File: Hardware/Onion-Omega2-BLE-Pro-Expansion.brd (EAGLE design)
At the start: 60 x 50 mm, 37 parts, among them J1 USB-MICROB, J2 USB-A-H, U2 ONION-OMEGA2

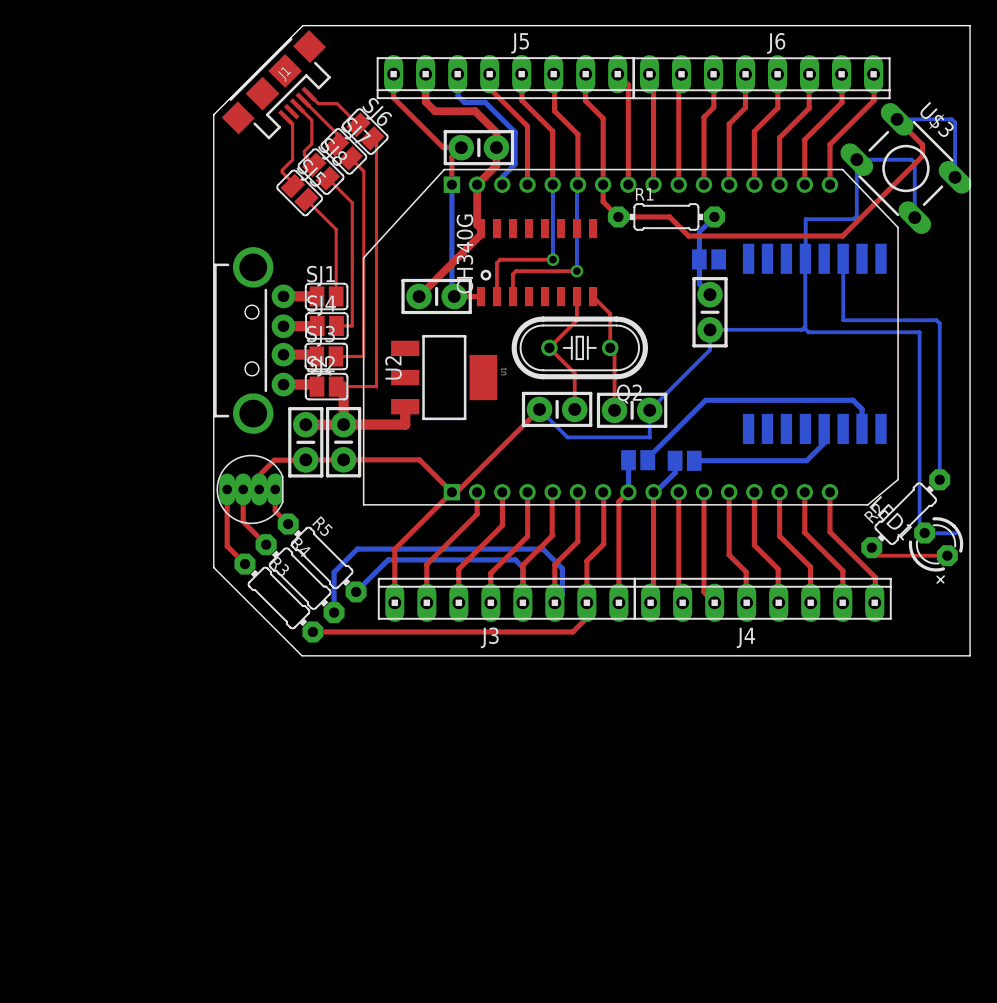
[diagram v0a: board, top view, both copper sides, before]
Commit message: Board Size reduced. Replaced almost all PTH with SMD. CH340G breakout. Minor improvements. Halfway manual routing. Lots of DRC errors
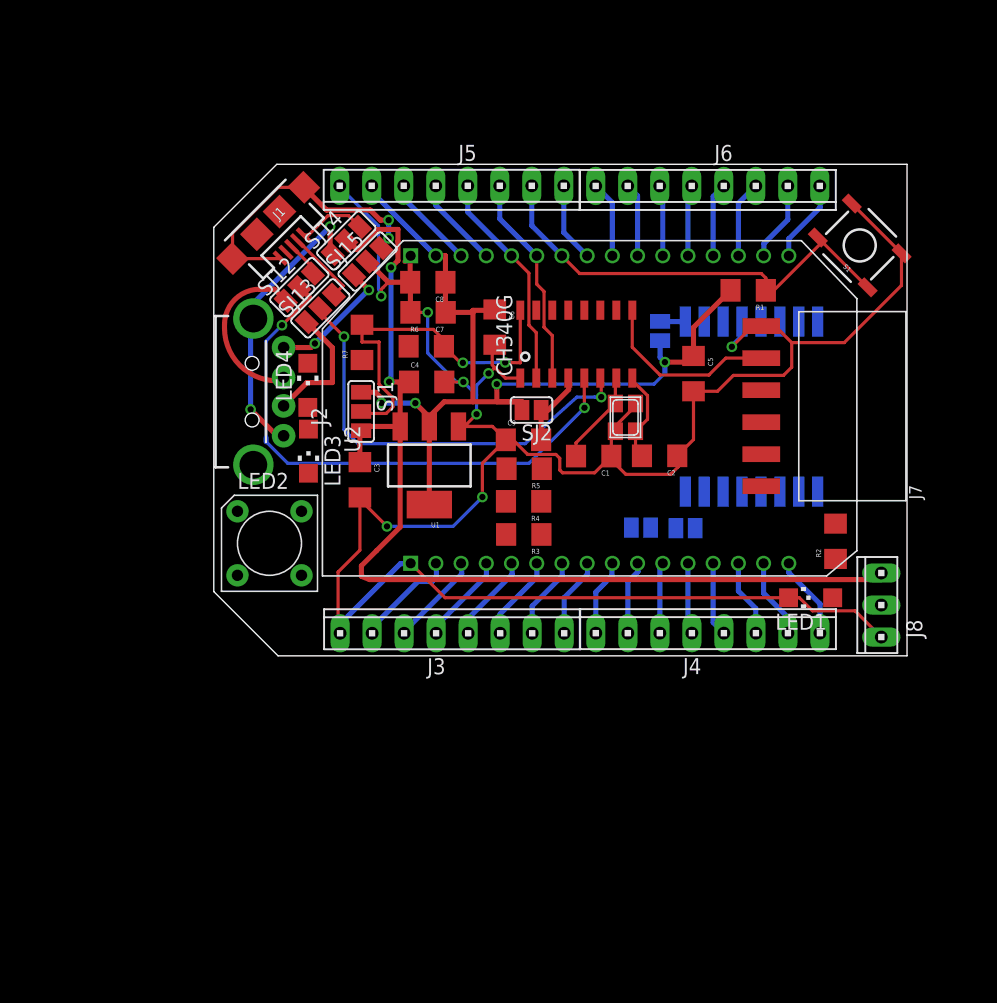
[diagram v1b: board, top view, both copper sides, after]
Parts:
- removed D1: LED-RGB-CC-THRUCLEAR, SparkFun-LED:LED-RGB-THRU
- removed Q2: (no value), adafruit:HC49U-V
- removed SJ3, SJ4, SJ5, SJ6, SJ7, SJ8: (no value), jumper:SJ
- removed U$3: TACTILE-SWITCH-PTH, GeekAmmo:TAC-SWITCH-PTH
- added C8: 10uF, SparkFun-Passives:1206
- added C9: 10nF, SparkFun-Passives:1206
- added J7: (no value), SparkFun-Connectors:1X06-SMD-FEMALE-V2
- added J8: (no value), con-amp:10X03MTA
- added LED2: RGBLED_CA-PIRANHA, adafruit:PIRANHA5MM
- added LED3, LED4: (no value), adafruit:CHIPLED_1206
- added Q1: 12Mhz 3225 Package, adafruit:NX3225
- added R6, R7: (no value), SparkFun-Passives:1206
- added S1: TAC_SWITCHSMD, SparkFun-Retired:TACTILE-SWITCH-SMD
- added SJ12, SJ13, SJ14, SJ15: (no value), jumper:SJ_2
- C1, C2, C3, C4, C5, C6, C7: device SparkFun-Capacitors:CAP-PTH-SMALL-KIT -> SparkFun-Passives:1206
- LED1: device adafruit:LED3MM -> adafruit:CHIPLED_1206
- R1, R2, R3, R4, R5: device adafruit:0204/7 -> SparkFun-Passives:1206
- SJ1: device jumper:SJ -> jumper:SJ_2
- moved R3 20.1 mm to (24.6, 9.63), turned to 180 degrees
- moved R4 18.8 mm to (24.6, 12.3), turned to 180 degrees
- moved R5 17.5 mm to (24.6, 14.8), turned to 180 degrees
- moved SJ2 16.4 mm to (25.2, 19.5), turned to 180 degrees
- moved C6 14.3 mm to (22.3, 26.1), turned to 270 degrees
- moved J1 11.2 mm to (4.32, 34.3)
- moved LED1 10.8 mm to (47.4, 4.61), turned to 90 degrees
- moved C4 10.7 mm to (16.9, 21.7), turned to 0 degrees
- moved J5 9.84 mm to (18.9, 37.3)
- moved J6 9.84 mm to (39.2, 37.3)
- moved SJ1 9.52 mm to (11.7, 19.4), turned to 270 degrees
- moved R1 8.72 mm to (42.4, 29.0), turned to 180 degrees
- moved U$1 7.18 mm to (28.8, 24.7)
- moved U1 7.08 mm to (17.1, 15.1), turned to 180 degrees
- moved U$2 7.07 mm to (41.9, 20.0)
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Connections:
- removed net N$10: D1.3, R4.1
- new net CTS: J7.2, U$1.9
- new net DTR: J7.6, U$1.13
- new net N$21: LED2.2, R3.2
- new net N$22: LED2.3, R4.2
- new net N$23: LED2.1, R5.2
- new net N$24: LED4.A, R7.1
- new net RX_340G: LED4.C
- new net VCC: J7.3, R6.2, R7.2, SJ1.2, U$1.16
- net 3.3V: now also C8.1, J8.2, LED2.4, SJ1.1, SJ2.2; no longer U$1.16, U$1.4
- net 5V: now also J8.1, SJ1.3, SJ14.2; no longer SJ2.2, SJ6.2
- net BLUE: now also R5.1; no longer R3.2
- net D+: now also SJ12.2; no longer SJ4.2, SJ8.2
- net D-: now also SJ13.2; no longer SJ3.2, SJ7.2
- net GND: now also C8.2, C9.1, J7.1, J8.3, LED1.C, Q1.2, Q1.4, S1.3, S1.4, SJ15.2; no longer D1.2, LED1.K, SJ1.2, SJ5.2, U$3.3, U$3.4
- net GREEN: now also R4.1; no longer R4.2
- net N$1: now also Q1.1; no longer Q2.2
- net N$11: now also LED3.A, R6.1; no longer D1.1, R5.1
- net N$2: now also Q1.3; no longer Q2.1
- net N$39: now also SJ15.1; no longer SJ1.1
- net N$40: now also SJ15.3; no longer SJ5.1
- net N$41: now also SJ14.3; no longer SJ6.1
- net N$42: now also SJ13.3; no longer SJ7.1
- net N$43: now also SJ12.3; no longer SJ8.1
- net N$44: now also SJ14.1; no longer SJ2.1
- net N$45: now also SJ13.1; no longer SJ3.1
- net N$46: now also SJ12.1; no longer SJ4.1
- net N$9: now also C9.2, SJ2.1, U$1.4; no longer D1.4, R3.1
- net RED: now also R3.1; no longer R5.2
- net RX_CH340: now also J7.5
- net TX_CH340: now also J7.4, LED3.C
- net Ω_RESET: now also S1.1, S1.2; no longer U$3.1, U$3.2
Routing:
- net 5V: track 35.4 -> 84.5 mm, vias 0 -> 2
- net 3.3V: track 31.7 -> 75.7 mm, vias 0 -> 4
- net GND: track 152.2 -> 192.3 mm, vias 0 -> 8
- net D+: track 13.8 -> 44.2 mm, vias 0 -> 2
- net VCC: track 0.00 -> 29.4 mm, vias 0 -> 2
- net GREEN: track 35.2 -> 6.76 mm
- net BLUE: track 32.8 -> 6.54 mm
- net N$3: track 25.0 -> 0.00 mm
- net N$5: track 20.9 -> 0.00 mm
- net RED: track 27.1 -> 7.02 mm
- net N$44: track 2.82 -> 22.9 mm, vias 0 -> 2
- net N$40: track 6.35 -> 23.2 mm, vias 0 -> 2
- net Ω_RESET: track 52.6 -> 36.1 mm
- net D-: track 18.4 -> 34.2 mm, vias 0 -> 2
- net CTS: track 0.00 -> 14.6 mm
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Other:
- board size 60 x 50 mm -> 55 x 39 mm

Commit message: Routing done with the help of autorouter. Not satisfied with few components placements
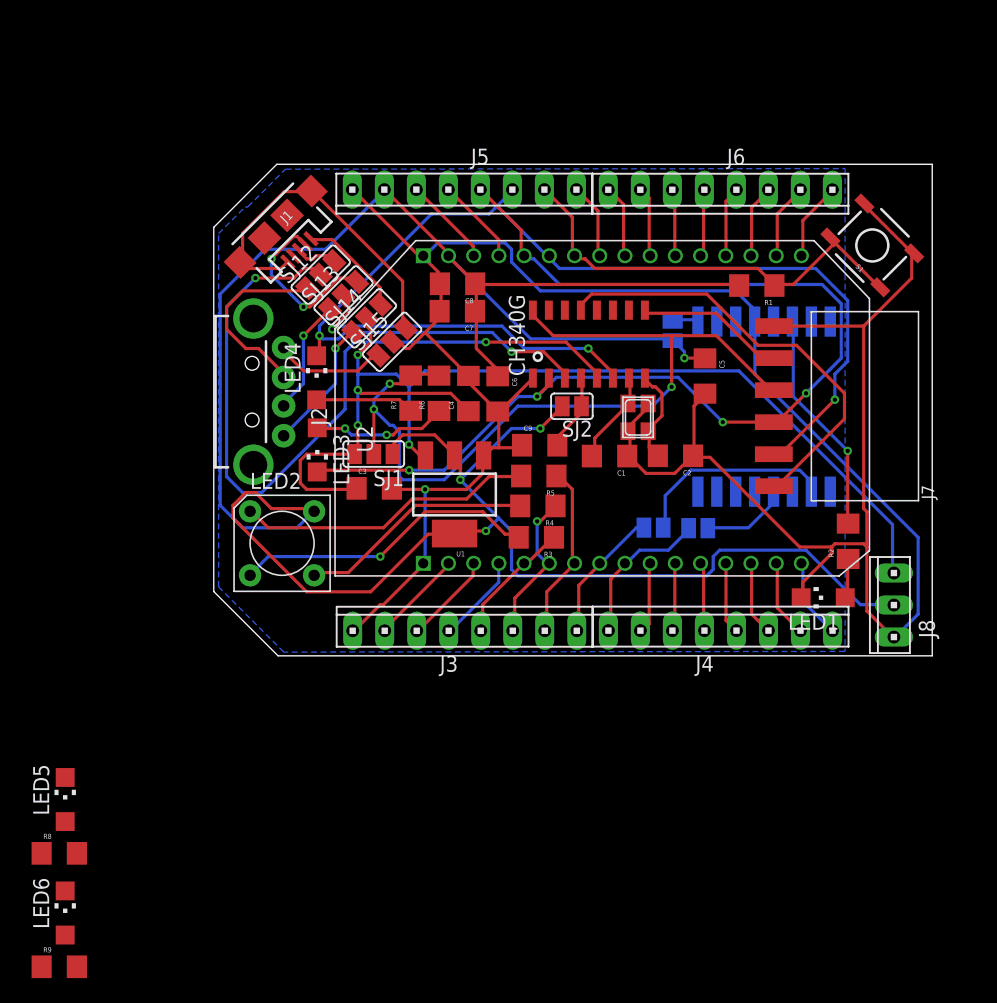
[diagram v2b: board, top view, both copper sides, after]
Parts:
- added LED5, LED6: (no value), adafruit:CHIPLED_1206
- added R8, R9: (no value), SparkFun-Passives:1206
- moved SJ15 6.66 mm to (14.1, 24.9)
- moved SJ14 6.39 mm to (12.1, 26.8)
- moved R7 5.58 mm to (15.6, 20.8)
- moved C6 5.30 mm to (22.5, 20.8)
- moved R6 3.86 mm to (17.9, 20.8), turned to 90 degrees
- moved SJ1 3.52 mm to (12.7, 16.0), turned to 180 degrees
- moved C4 3.44 mm to (20.2, 20.8), turned to 90 degrees
- moved SJ2 3.21 mm to (28.4, 19.8)
- moved U1 3.05 mm to (19.1, 12.8)
- moved C8 2.36 mm to (19.3, 29.5)
- moved C7 2.32 mm to (19.3, 27.3)
- moved SJ13 2.11 mm to (10.3, 28.6)
- moved SJ12 1.97 mm to (8.49, 30.2)
- moved C9 1.36 mm to (25.9, 16.7)
- moved C3 1.33 mm to (12.7, 13.3), turned to 0 degrees
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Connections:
- removed net RX_340G: LED4.C
- new net N$25: LED5.A, R8.1
- new net N$26: LED6.A, R9.1
- net 3.3V: now also R9.2
- net 5V: now also R8.2
- net GND: now also LED5.C, LED6.C
- net RX_CH340: now also LED4.C
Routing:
- net 3.3V: track 75.7 -> 202.2 mm
- net RX_CH340: track 17.0 -> 89.9 mm, vias 0 -> 3
- net TX_CH340: track 17.5 -> 88.4 mm, vias 0 -> 4
- net VCC: track 29.4 -> 67.5 mm, vias 2 -> 3
- net DTR: track 0.00 -> 35.2 mm
- net N$21: track 0.00 -> 24.3 mm, vias 0 -> 1
- net N$23: track 0.00 -> 23.8 mm
- net N$22: track 0.00 -> 18.7 mm
- net N$3: track 0.00 -> 17.8 mm, vias 0 -> 1
- net D+: track 44.2 -> 61.4 mm
- net N$5: track 0.00 -> 16.2 mm
- net GND: track 192.3 -> 207.0 mm, vias 8 -> 1
- net N$44: track 22.9 -> 10.6 mm, vias 2 -> 1
- net N$11: track 0.00 -> 10.7 mm, vias 0 -> 2
- net N$24: track 0.00 -> 7.82 mm
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- added copper zone on layer 16, net N$10
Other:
- board size 55 x 39 mm -> 57 x 39 mm

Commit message: v0.1 freeze. Placements looks good.
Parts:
- moved R9 41.4 mm to (12.7, 8.41), turned to 180 degrees
- moved LED6 39.2 mm to (18.1, 5.00), turned to 90 degrees
- moved R8 36.4 mm to (12.7, 10.8), turned to 180 degrees
- moved LED5 29.5 mm to (12.7, 5.05), turned to 90 degrees
- moved U$2 6.67 mm to (49.6, 19.6)
- moved J2 1.47 mm to (3.11, 19.5)
- moved LED2 1.39 mm to (5.38, 7.54)
- moved J7 1.14 mm to (49.0, 19.5)
- moved LED1 0.47 mm to (48.4, 5.08)
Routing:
- net 3.3V: track 202.2 -> 141.2 mm, vias 4 -> 5
- net RX_CH340: track 89.9 -> 64.2 mm
- net N$26: track 0.00 -> 20.1 mm, vias 0 -> 2
- net VCC: track 67.5 -> 47.9 mm, vias 3 -> 5
- net N$21: track 24.3 -> 42.6 mm, vias 1 -> 0
- net GND: track 207.0 -> 189.3 mm, vias 1 -> 5
- net N$45: track 9.19 -> 26.8 mm, vias 1 -> 0
- net 5V: track 90.5 -> 106.3 mm, vias 4 -> 5
- net D+: track 61.4 -> 72.8 mm, vias 2 -> 4
- net D-: track 27.7 -> 38.9 mm, vias 2 -> 4
- net TX_CH340: track 88.4 -> 77.3 mm, vias 4 -> 2
- net N$13: track 2.15 -> 11.1 mm
- net N$5: track 16.2 -> 24.4 mm, vias 0 -> 2
- net DTR: track 35.2 -> 27.7 mm, vias 0 -> 2
- net N$25: track 0.00 -> 7.35 mm
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
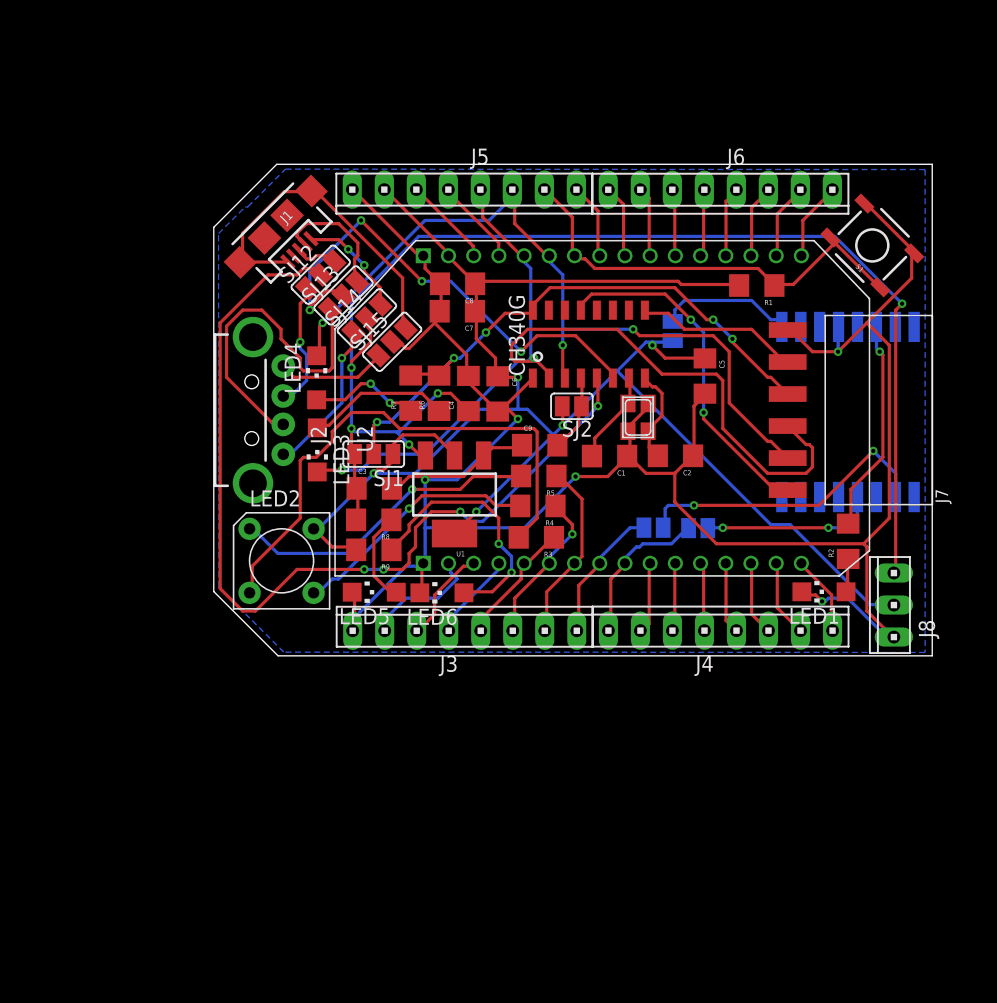
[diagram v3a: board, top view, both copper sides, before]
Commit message: Silk Screen Fix
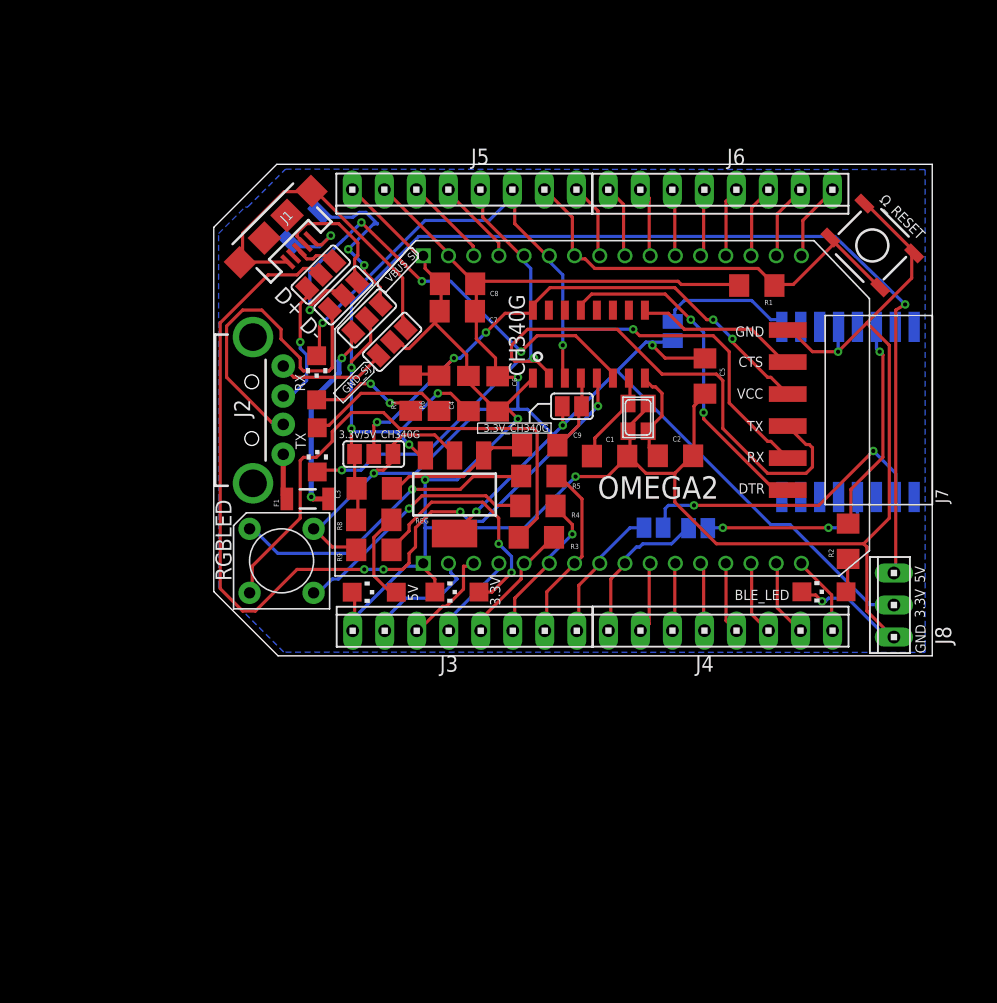
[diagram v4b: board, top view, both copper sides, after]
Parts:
- removed LED6: (no value), adafruit:CHIPLED_1206
- added 3.3V: (no value), adafruit:CHIPLED_1206
- added F1, F2: PTCSMD-W, SparkFun-PowerIC:PTC-1206-WIDE
- renumbered LED1 to BLE_LED, LED2 to RGBLED, LED3 to TX, LED4 to RX, LED5 to 5V, S1 to Ω_RESET, SJ1 to 3.3V/5V_CH340G, SJ10 to Ω_TX1, SJ11 to 3.3V_HM11, SJ12 to D+, SJ13 to D-, SJ14 to VBUS_SJ, SJ15 to GND_SJ, SJ2 to 3.3V_CH340G, SJ9 to Ω_RX1, U1 to REG, U2 to OMEGA2
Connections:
- new net N$27: F2.1, J1.VBUS
- new net N$37: F1.1, J2.VBUS
- new net RTS: U$1.14
- net GND: now also 3.3V.C; no longer LED6.C
- net N$26: now also 3.3V.A; no longer LED6.A
- net N$41: now also F2.2; no longer J1.VBUS
- net N$44: now also F1.2; no longer J2.VBUS
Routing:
- net N$27: track 0.00 -> 5.83 mm, vias 0 -> 1
- net N$41: track 8.74 -> 13.9 mm
- net N$37: track 0.00 -> 3.95 mm
- net N$44: track 12.4 -> 16.0 mm, vias 1 -> 2
- net N$26: track 20.1 -> 18.9 mm
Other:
- board text added: "11"
- board text added: "15"
- board text added: "16"
- board text added: "17"
- board text added: "18"
- board text added: "19"
- board text added: "3.3V"
- board text added: "5V"
- board text added: "CLK"
- board text added: "CS1"
- board text added: "CTS"
- board text added: "D+"
- board text added: "D-"
- board text added: "DTR"
- board text added: "Designed and Assembled in India. Manufactured in China."
- board text added: "Designed by Github/Vijayenthiran"
- board text added: "Ethernet"
- board text added: "FWRST"
- board text added: "GND"
- board text added: "I2C"
- board text added: "I2S"
- board text added: "MISO"
- board text added: "MOSI"
- board text added: "RST"
- board text added: "RX"
- board text added: "RX+"
- board text added: "RX-"
- board text added: "RX0"
- board text added: "RX1"
- board text added: "SCL"
- board text added: "SDA"
- board text added: "SDI"
- board text added: "SDO"
- board text added: "SPI"
- board text added: "Serial"
- board text added: "TX"
- board text added: "TX+"
- board text added: "TX-"
- board text added: "TX0"
- board text added: "TX1"
- board text added: "USB"
- board text added: "VCC"
- board text added: "VOUT"
- board text added: "WS"
